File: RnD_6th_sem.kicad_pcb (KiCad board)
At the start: 4 copper layers, 69.8 x 71.1 mm, 58 parts, among them IC1 2EDF7275KXUMA1, J1 HVDC1, J2 PWM, J3 HVDC2, J4 3.3V, J5 5V, J6 5V, J7 GND2, J8 GND1, Q1 IGLD60R190D1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

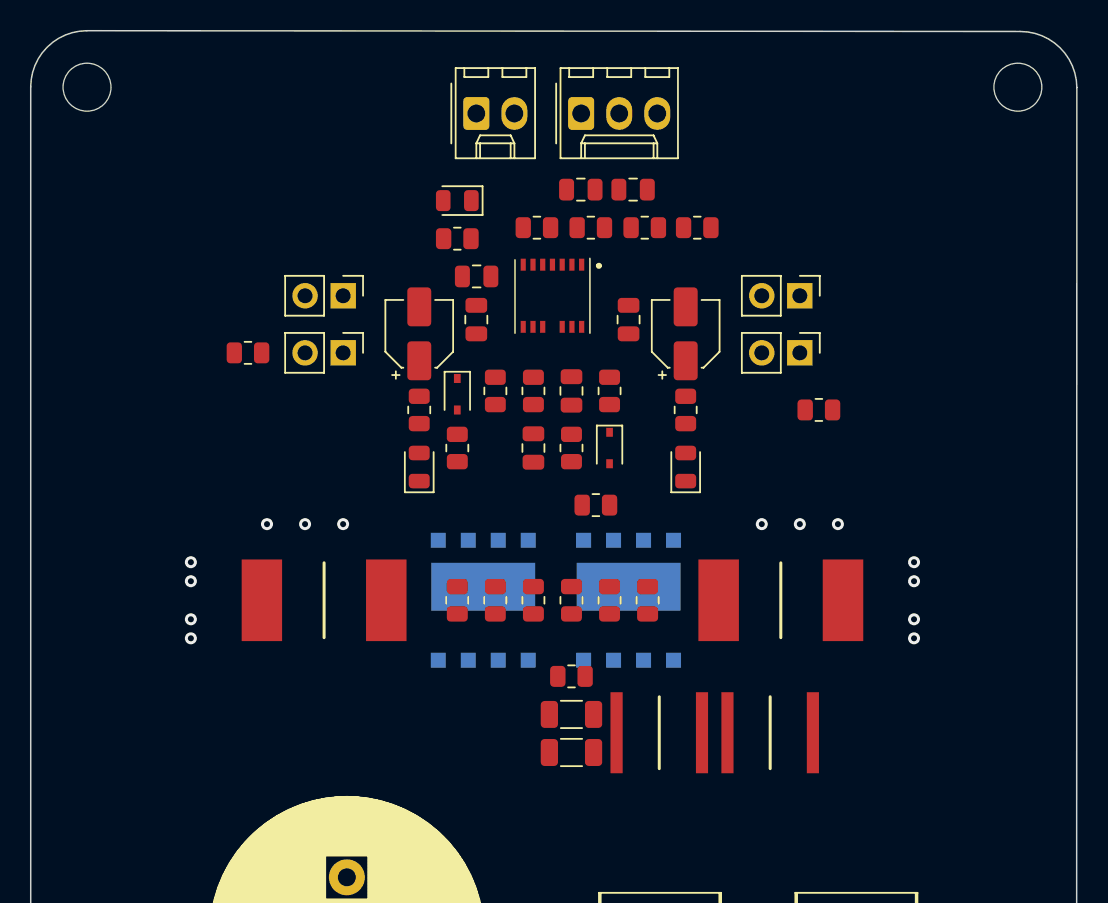
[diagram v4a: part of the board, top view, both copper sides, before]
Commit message: updated the schematic
removed the mmcx connector resistors
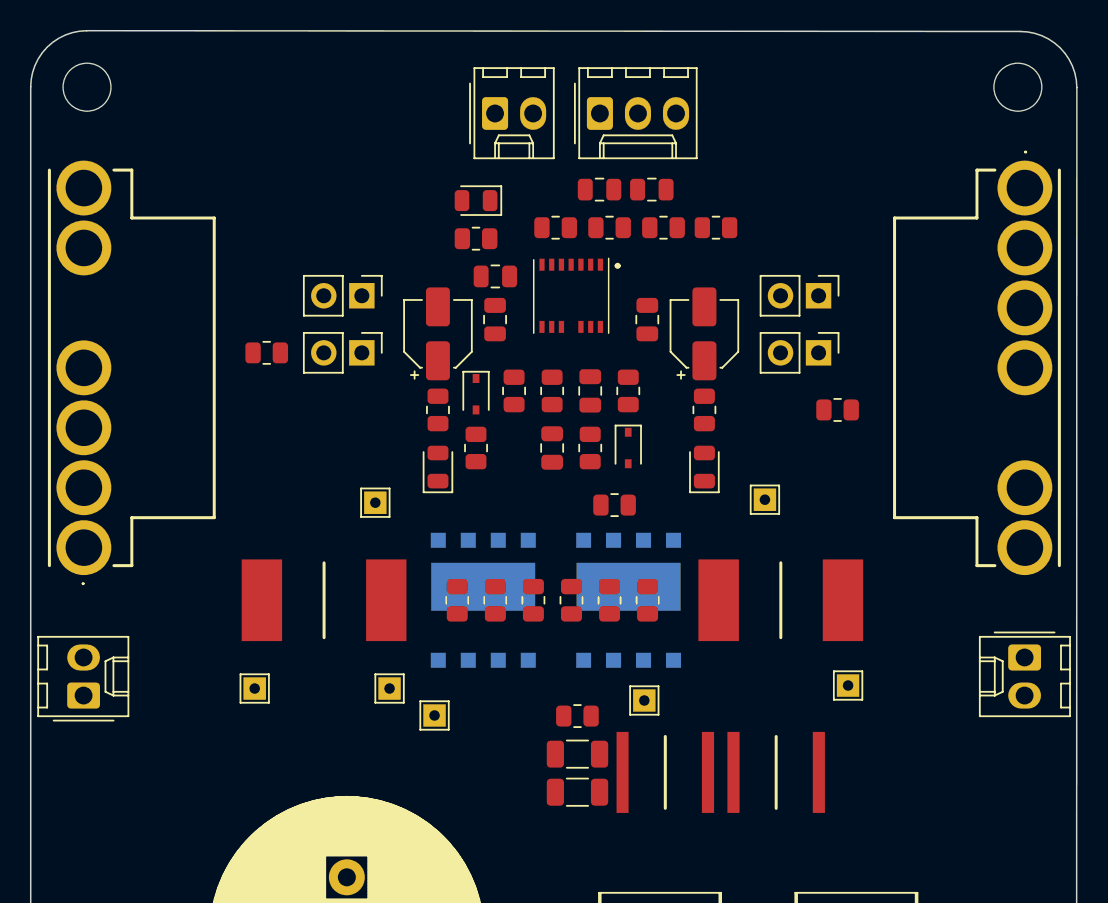
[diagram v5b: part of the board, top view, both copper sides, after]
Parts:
- added J10: To_amplifier, Connector_Molex:Molex_KK-254_AE-6410-02A_1x02_P2.54mm_Vertical, F.Cu at (105.2, 92.7)
- added J9: To_amplifier, Connector_Molex:Molex_KK-254_AE-6410-02A_1x02_P2.54mm_Vertical, F.Cu at (168.0, 90.1)
- added PS1: LS05-13B05R3, footprint&lib:LS0513B05R3, F.Cu at (105.2, 82.8)
- added PS2: LS05-13B05R3, footprint&lib:LS0513B05R3, F.Cu at (168.0, 58.8)
- added TP1: TestPoint_Alt, TestPoint:TestPoint_THTPad_1.5x1.5mm_Drill0.7mm, F.Cu at (150.7, 79.6)
- added TP2: TestPoint_Alt, TestPoint:TestPoint_THTPad_1.5x1.5mm_Drill0.7mm, F.Cu at (124.7, 79.8)
- added TP3: TestPoint_Alt, TestPoint:TestPoint_THTPad_1.5x1.5mm_Drill0.7mm, F.Cu at (142.6, 93.0)
- added TP4: TestPoint_Alt, TestPoint:TestPoint_THTPad_1.5x1.5mm_Drill0.7mm, F.Cu at (128.6, 94.0)
- added TP5: TestPoint_Alt, TestPoint:TestPoint_THTPad_1.5x1.5mm_Drill0.7mm, F.Cu at (125.6, 92.2)
- added TP6: TestPoint_Alt, TestPoint:TestPoint_THTPad_1.5x1.5mm_Drill0.7mm, F.Cu at (156.2, 92.0)
- added TP7: TestPoint_Alt, TestPoint:TestPoint_THTPad_1.5x1.5mm_Drill0.7mm, F.Cu at (116.6, 92.2)
- moved C7 2.68 mm to (138.1, 99.1)
- moved R8 2.68 mm to (138.1, 94.0)
- moved C8 2.68 mm to (144.0, 97.8)
- moved C9 2.68 mm to (151.4, 97.8)
- moved C6 2.68 mm to (138.1, 96.6)
- moved C16 1.25 mm to (128.8, 68.5)
- moved D7 1.25 mm to (128.8, 77.4)
- moved R12 1.25 mm to (128.8, 73.6)
- moved C1 1.25 mm to (132.7, 64.7)
- moved C13 1.25 mm to (139.6, 58.9)
- moved C14 1.25 mm to (143.1, 58.9)
- moved C15 1.25 mm to (146.6, 68.5)
- moved C2 1.25 mm to (142.8, 67.6)
- moved C3 1.25 mm to (132.6, 67.6)
- moved C4 1.25 mm to (139.0, 72.3)
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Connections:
- C4 pad 1: OUTA -> OUTB
- D1 pad 1: OUTB -> OUTA
- Q1 pad 8: Net-(Q1-Pad8) -> Net-(C5-Pad2)
- Q2 pad 5: Net-(Q2-Pad5) -> Net-(J10-Pad2)
- Q2 pad 6: Net-(Q2-Pad5) -> Net-(J10-Pad2)
- Q2 pad 8: Net-(C5-Pad2) -> Net-(Q2-Pad8)
- Q2 pad 9: Net-(Q2-Pad5) -> Net-(J10-Pad2)
- R1 pad 1: OUTA -> OUTB
- R1 pad 2: Net-(Q1-Pad8) -> Net-(Q2-Pad8)
- R2 pad 1: OUTB -> OUTA
- R3 pad 1: OUTB -> OUTA
- R4 pad 2: Net-(Q1-Pad8) -> Net-(Q2-Pad8)
- R6 pad 2: Net-(Q1-Pad8) -> Net-(Q2-Pad8)
- R9 pad 1: Net-(R17-Pad2) -> Net-(J10-Pad2)
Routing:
- net (no net): vias 14 -> 0

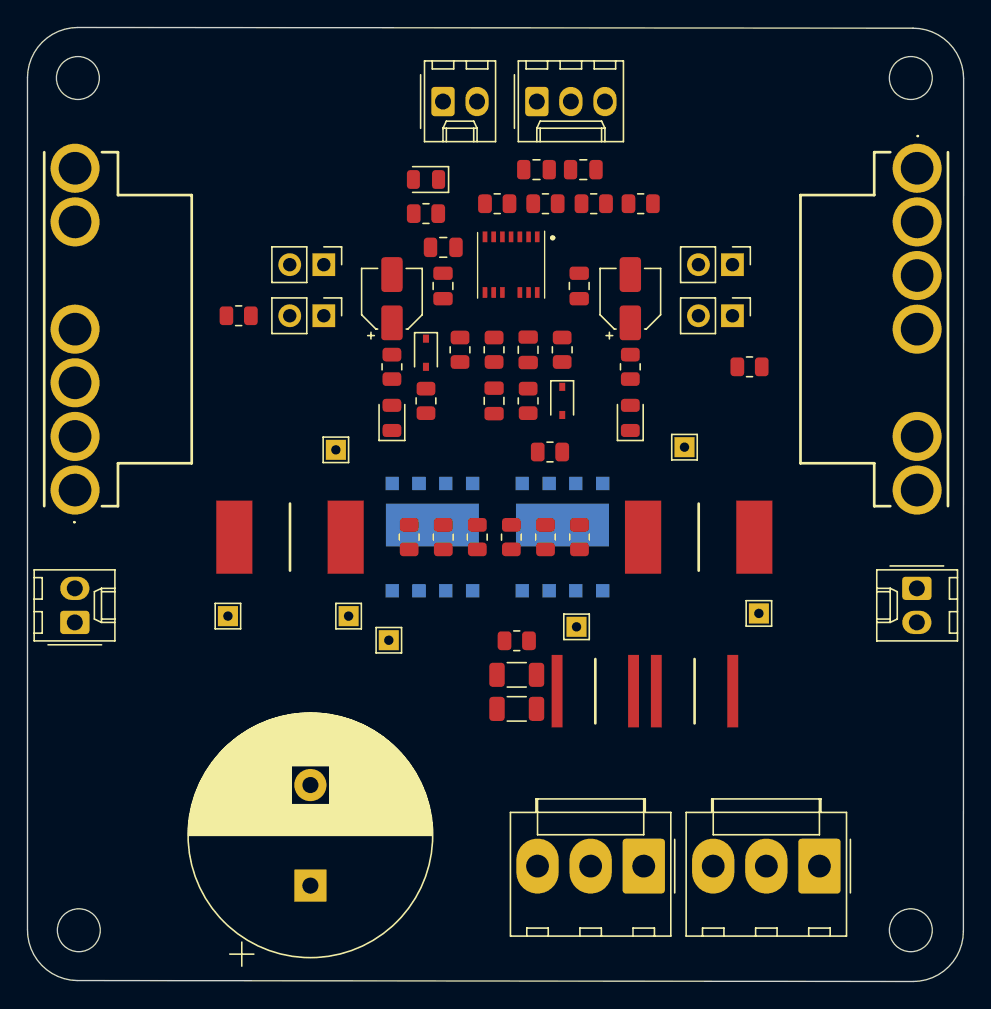
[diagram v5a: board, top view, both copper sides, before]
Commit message: trace routing partially completed
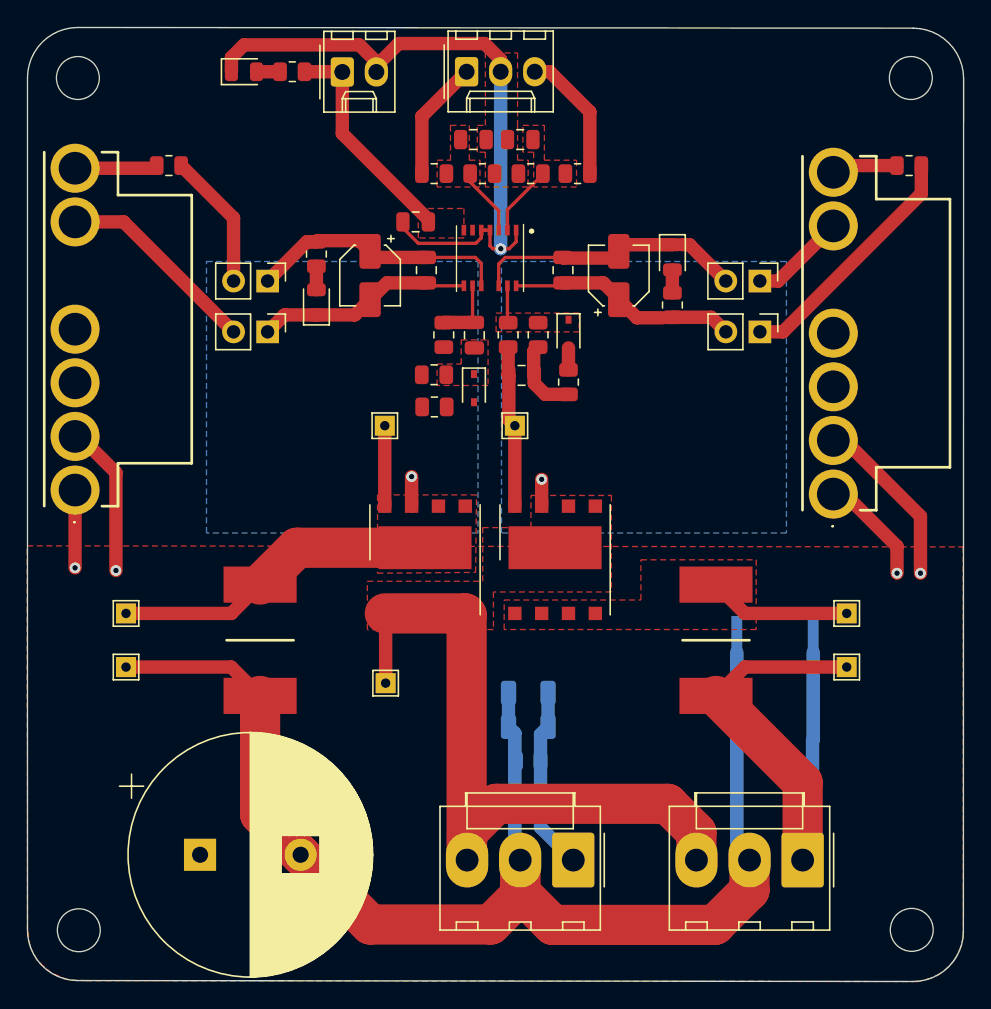
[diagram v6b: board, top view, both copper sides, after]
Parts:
- removed J10, J9: To_amplifier, Connector_Molex:Molex_KK-254_AE-6410-02A_1x02_P2.54mm_Vertical
- removed R17, R18, R19, R20: 1R, Resistor_SMD:R_0805_2012Metric
- removed R21, R22: NC, Resistor_SMD:R_0805_2012Metric
- C6, C7, C8, C9, R8: moved to B.Cu
- Q1, Q2: moved to F.Cu
- moved PS2 67.2 mm to (105.2, 82.8), turned to 90 degrees
- moved PS1 56.6 mm to (161.8, 83.1)
- moved TP3 20.2 mm to (162.8, 92.0)
- moved FB4 19.2 mm to (167.4, 58.6)
- moved TP5 16.6 mm to (109.0, 92.0)
- moved D5 15.8 mm to (117.8, 51.6), turned to 0 degrees
- moved R10 14.5 mm to (121.4, 51.6)
- moved C8 13.9 mm to (157.4, 101.4), turned to 180 degrees
- moved TP1 12.8 mm to (138.0, 78.0)
- moved D6 12.4 mm to (149.8, 65.4), turned to -90 degrees
- moved FB3 12.3 mm to (112.2, 58.6)
- moved D1 10.7 mm to (142.0, 71.1)
- moved R5 10.7 mm to (142.0, 74.8), turned to -90 degrees
- moved D7 10.3 mm to (123.2, 68.8)
- moved R12 10.1 mm to (123.2, 65.2)
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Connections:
- C15 pad 2: Net-(C15-Pad2) -> gnd-1
- C16 pad 2: Net-(C16-Pad2) -> gnd-2
- C2 pad 1: Net-(C15-Pad2) -> gnd-1
- C3 pad 1: Net-(C16-Pad2) -> gnd-2
- D6 pad 1: GND1 -> gnd-1
- D7 pad 1: GND2 -> gnd-2
- IC1 pad 11: Net-(C15-Pad2) -> gnd-1
- IC1 pad 8: Net-(C16-Pad2) -> gnd-2
- J1 pad 1: Net-(J1-Pad1) -> HVDC+
- J1 pad 3: HVDC+ -> Net-(J1-Pad3)
- J3 pad 1: Net-(J1-Pad1) -> HVDC+
- J3 pad 3: HVDC+ -> Net-(J1-Pad3)
- J7 pad 1: Net-(C16-Pad2) -> gnd-2
- J8 pad 2: Net-(C15-Pad2) -> gnd-1
- Q1 pad 5: Net-(J1-Pad1) -> Net-(J1-Pad3)
- Q1 pad 6: Net-(J1-Pad1) -> Net-(J1-Pad3)
- Q1 pad 7: GND1 -> gnd-1
- Q1 pad 9: Net-(J1-Pad1) -> Net-(J1-Pad3)
- Q2 pad 1: Net-(J1-Pad1) -> Net-(J1-Pad3)
- Q2 pad 2: Net-(J1-Pad1) -> Net-(J1-Pad3)
- Q2 pad 3: Net-(J1-Pad1) -> Net-(J1-Pad3)
- Q2 pad 4: Net-(J1-Pad1) -> Net-(J1-Pad3)
- Q2 pad 7: GND2 -> gnd-2
- TP4 pad 1: Net-(J1-Pad1) -> Net-(J1-Pad3)
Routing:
- net GND3: track 0.00 -> 123.2 mm, vias 0 -> 2
- net HVDC+: track 0.00 -> 69.3 mm, vias 0 -> 2
- net Net-(J1-Pad3): track 0.00 -> 52.6 mm
- net GND: track 0.00 -> 51.0 mm, vias 0 -> 1
- net Net-(Q2-Pad5): track 0.00 -> 24.3 mm
- net gnd-1: track 0.00 -> 21.6 mm, vias 0 -> 1
- net LED2: track 0.00 -> 19.6 mm
- net gnd-2: track 0.00 -> 18.4 mm, vias 0 -> 1
- net VCCA: track 0.00 -> 18.4 mm
- net +3.3V: track 0.00 -> 16.7 mm
- net LED1: track 0.00 -> 16.6 mm
- net GND2: track 0.00 -> 15.2 mm
- net Net-(C5-Pad2): track 0.00 -> 12.1 mm
- net Net-(Q1-Pad1): track 0.00 -> 10.8 mm
- net VCCB: track 0.00 -> 10.2 mm
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- added copper zone on F.Cu, net +3.3V
- added copper zone on F.Cu, net GND
- added copper zone on F.Cu, net GND3
- added copper zone on In1.Cu, net GND3
- added copper zone on In2.Cu, net HVDC+
- added copper zone on F.Cu, net Net-(C4-Pad2)
- added copper zone on F.Cu, net Net-(J1-Pad3)
- added copper zone on F.Cu, net Net-(Q1-Pad1)
- added copper zone on F.Cu, net Net-(Q2-Pad5)
- added copper zone on F.Cu, net OUTA
- added copper zone on F.Cu, net PWM1
- added copper zone on F.Cu, net PWM2
- added copper zone on B.Cu, net gnd-1
- added copper zone on B.Cu, net gnd-2

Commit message: changed layout
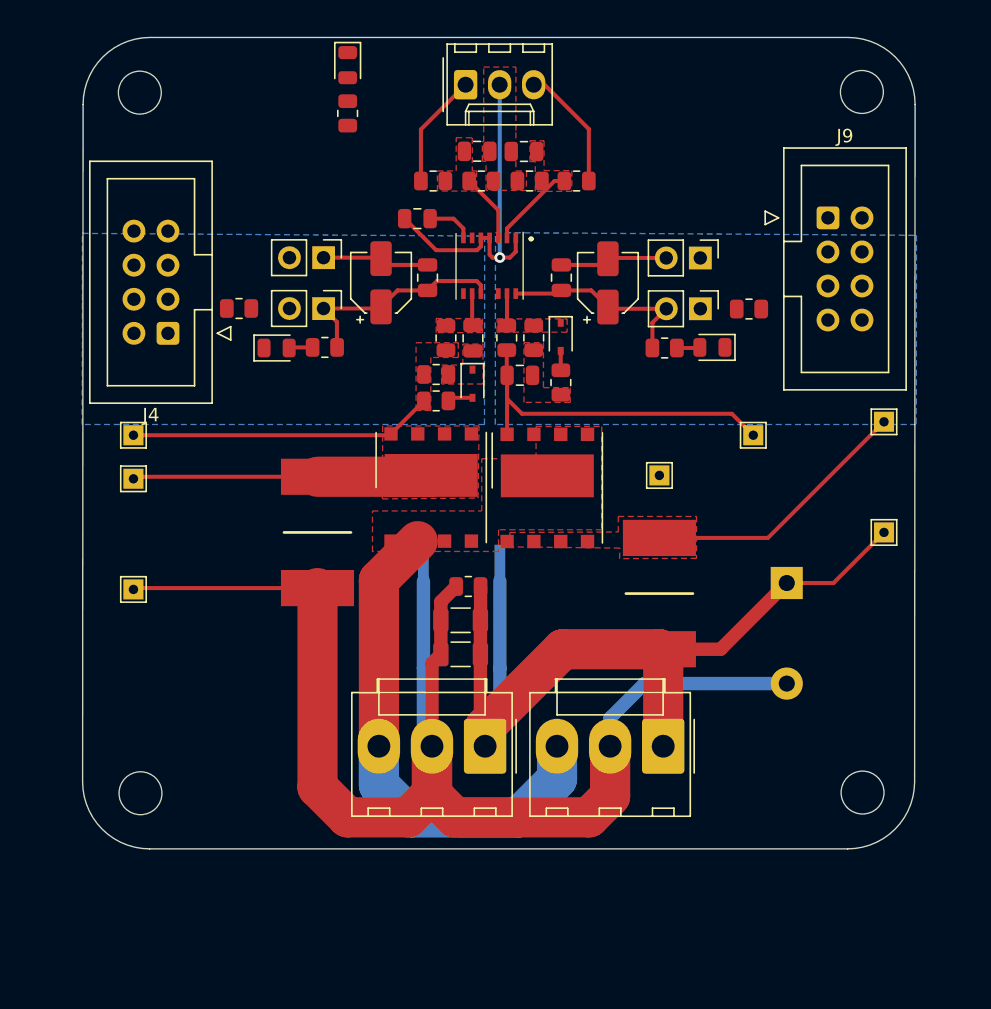
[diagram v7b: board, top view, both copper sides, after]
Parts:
- removed PS1, PS2: LS05-13B05R3, footprint&lib:LS0513B05R3
- added J9: Conn_02x04_Odd_Even, Connector_IDC:IDC-Header_2x04_P2.54mm_Vertical, F.Cu at (161.3, 62.5)
- C10: moved to B.Cu
- C6, C7: value 100nF/630V -> 100nF/450V; moved to F.Cu
- J4: value 3.3V -> Conn_02x04_Odd_Even; footprint Connector_Molex:Molex_KK-254_AE-6410-02A_1x02_P2.54mm_Vertical -> Connector_IDC:IDC-Header_2x04_P2.54mm_Vertical
- R8: moved to F.Cu
- moved C10 48.2 mm to (158.3, 89.7), turned to -90 degrees
- moved TP4 25.6 mm to (148.8, 81.7)
- moved C8 24.0 mm to (134.0, 96.1)
- moved C9 24.0 mm to (134.0, 89.6)
- moved J4 23.4 mm to (112.1, 71.1), turned to 180 degrees
- moved TP2 18.8 mm to (109.6, 78.7)
- moved TP1 17.8 mm to (155.8, 78.7)
- moved FB4 16.0 mm to (155.5, 69.3), turned to 180 degrees
- moved TP3 14.6 mm to (165.5, 77.7)
- moved R8 13.8 mm to (134.5, 90.0)
- moved J1 13.4 mm to (149.1, 101.9)
- moved FB3 11.9 mm to (117.4, 69.3)
- moved H2 11.2 mm to (110.1, 105.4)
- moved H1 10.9 mm to (163.9, 105.4)
- moved J3 10.7 mm to (135.8, 101.9)
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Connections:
- J4 pad 1: +3.3V -> Net-(FB4-Pad1)
- J4 pad 2: GND -> Net-(FB4-Pad1)
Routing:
- net GND: track 51.0 -> 25.5 mm
- net VCCA: track 18.4 -> 0.00 mm
- net GND3: track 123.2 -> 105.9 mm, vias 2 -> 0
- net Net-(Q2-Pad8): track 6.00 -> 22.7 mm
- net Net-(C5-Pad2): track 12.1 -> 27.5 mm
- net Net-(J1-Pad3): track 52.6 -> 37.3 mm
- net GND2: track 15.2 -> 0.00 mm
- net gnd-1: track 21.6 -> 8.04 mm, vias 1 -> 0
- net +3.3V: track 16.7 -> 3.49 mm
- net gnd-2: track 18.4 -> 7.98 mm, vias 1 -> 0
- net VCCB: track 10.2 -> 0.00 mm
- net Net-(Q1-Pad1): track 10.8 -> 20.3 mm
- net GND1: track 7.18 -> 0.00 mm
- net Net-(FB3-Pad1): track 6.17 -> 0.00 mm
- net Net-(C5-Pad1): track 5.76 -> 0.00 mm
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- added copper zone on F.Cu, net Net-(C5-Pad1)
- added copper zone on F.Cu, net Net-(Q2-Pad8)
- added copper zone on F.Cu, net OUTB
- removed copper zone on F.Cu, net +3.3V
- removed copper zone on F.Cu, net GND3
- removed copper zone on In1.Cu, net GND3
- removed copper zone on In2.Cu, net HVDC+
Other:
- board size 69.8 x 71.1 mm -> 62.1 x 60.5 mm
- copper layers 4 -> 2
- board text added: "keep everything closer add common mode choke use smaller track check new power bricks"

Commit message: added power board files
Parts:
- added FB1: fb, Resistor_SMD:R_0805_2012Metric, F.Cu at (155.5, 65.5)
- added FB2: fb, Resistor_SMD:R_0805_2012Metric, F.Cu at (117.4, 65.5)
- added N1: Housing, Symbol:KiCad-Logo_20mm_SilkScreen, F.Cu at (135.3, 64.5)
- J4, J9: footprint Connector_IDC:IDC-Header_2x04_P2.54mm_Vertical -> Connector_PinSocket_2.54mm:PinSocket_2x04_P2.54mm_Vertical
- moved J4 54.3 mm to (165.6, 61.6), turned to 0 degrees
- moved J9 53.8 mm to (108.0, 69.2), turned to 180 degrees
- moved D5 19.2 mm to (107.8, 58.5), turned to 0 degrees
- moved R10 14.6 mm to (111.4, 58.5), turned to 0 degrees
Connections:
- J4 pad 1: Net-(FB4-Pad1) -> unconnected-(J4-Pad1)
- J4 pad 2: Net-(FB4-Pad1) -> unconnected-(J4-Pad2)
- J4 pad 3: GND1 -> unconnected-(J4-Pad3)
- J4 pad 4: GND1 -> unconnected-(J4-Pad4)
- J4 pad 5: +3.3V -> Net-(FB1-Pad2)
- J4 pad 6: +3.3V -> Net-(FB1-Pad2)
- J4 pad 7: GND -> Net-(FB4-Pad1)
- J4 pad 8: GND -> Net-(FB4-Pad1)
- J9 pad 3: GND2 -> Net-(FB2-Pad1)
- J9 pad 4: GND2 -> Net-(FB2-Pad1)
- J9 pad 5: unconnected-(J9-Pad5) -> GND
- J9 pad 6: unconnected-(J9-Pad6) -> GND
- J9 pad 7: unconnected-(J9-Pad7) -> +3.3V
- J9 pad 8: unconnected-(J9-Pad8) -> +3.3V
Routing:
- net GND: track 25.5 -> 54.4 mm
- net +3.3V: track 3.49 -> 32.0 mm
- net Net-(FB1-Pad2): track 0.00 -> 9.77 mm
- net Net-(FB4-Pad1): track 0.00 -> 9.26 mm
- net Net-(FB2-Pad1): track 0.00 -> 9.05 mm
- net gnd-1: track 8.04 -> 16.7 mm, vias 0 -> 12
- net Net-(FB3-Pad1): track 0.00 -> 8.55 mm
- net Net-(J1-Pad3): track 37.3 -> 45.7 mm
- net gnd-2: track 7.98 -> 15.0 mm, vias 0 -> 12
- net VCCB: track 0.00 -> 2.85 mm
- net GND2: track 0.00 -> 2.84 mm
- net GND1: track 0.00 -> 2.73 mm
- net VCCA: track 0.00 -> 2.72 mm
- net Net-(D5-Pad2): track 0.00 -> 1.75 mm
